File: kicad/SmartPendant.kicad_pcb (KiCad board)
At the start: 2 copper layers, 125 x 59 mm, 49 parts, among them J1 UART, J2 ST-LINK, J3 Encoder, J4 Display, J5 USB_C_Receptacle_USB2.0_16P, J6 Micro_SD_Card_Det1, Q1 MMBT3904, U1 WEACT BLACKPILL F4X1, U2 AMS1117-3.3, U3 MB85RC256VPNF-G-JNERE1

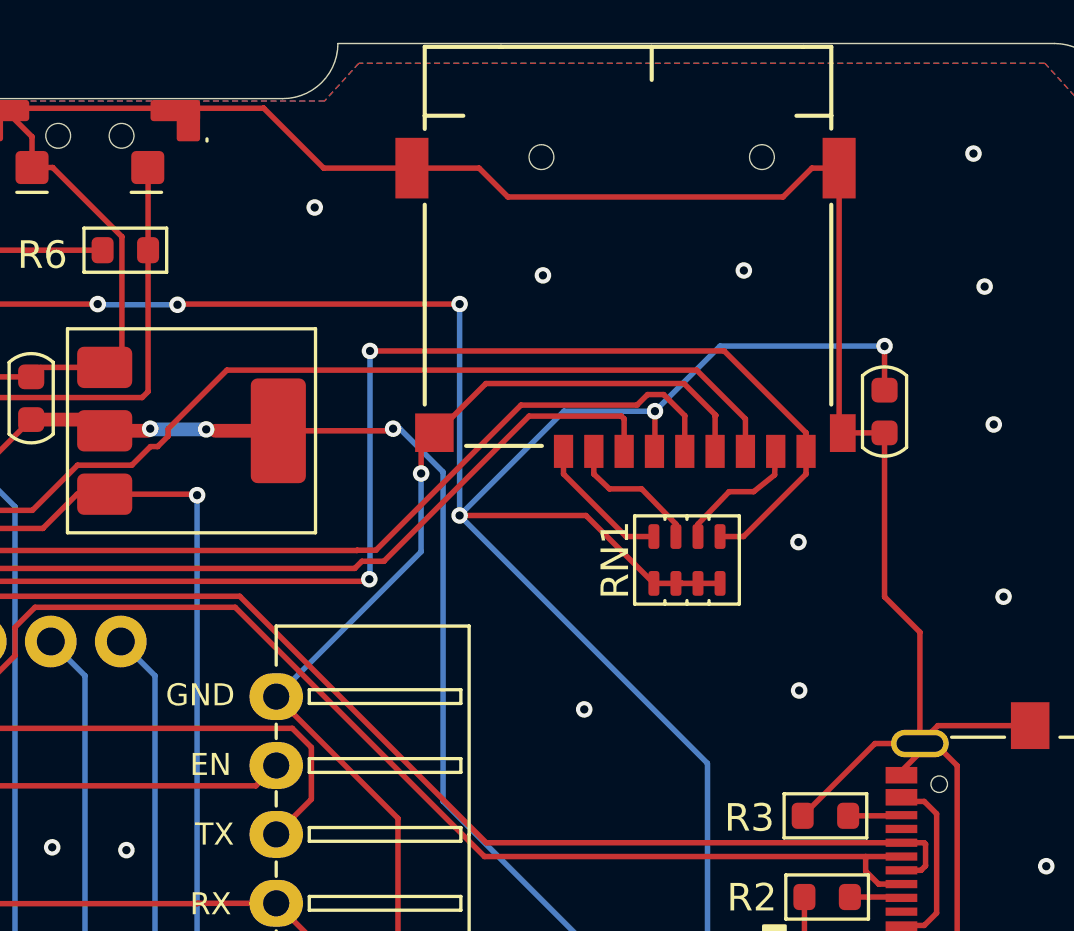
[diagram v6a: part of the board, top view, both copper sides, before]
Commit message: Use dual SD-card footprint.
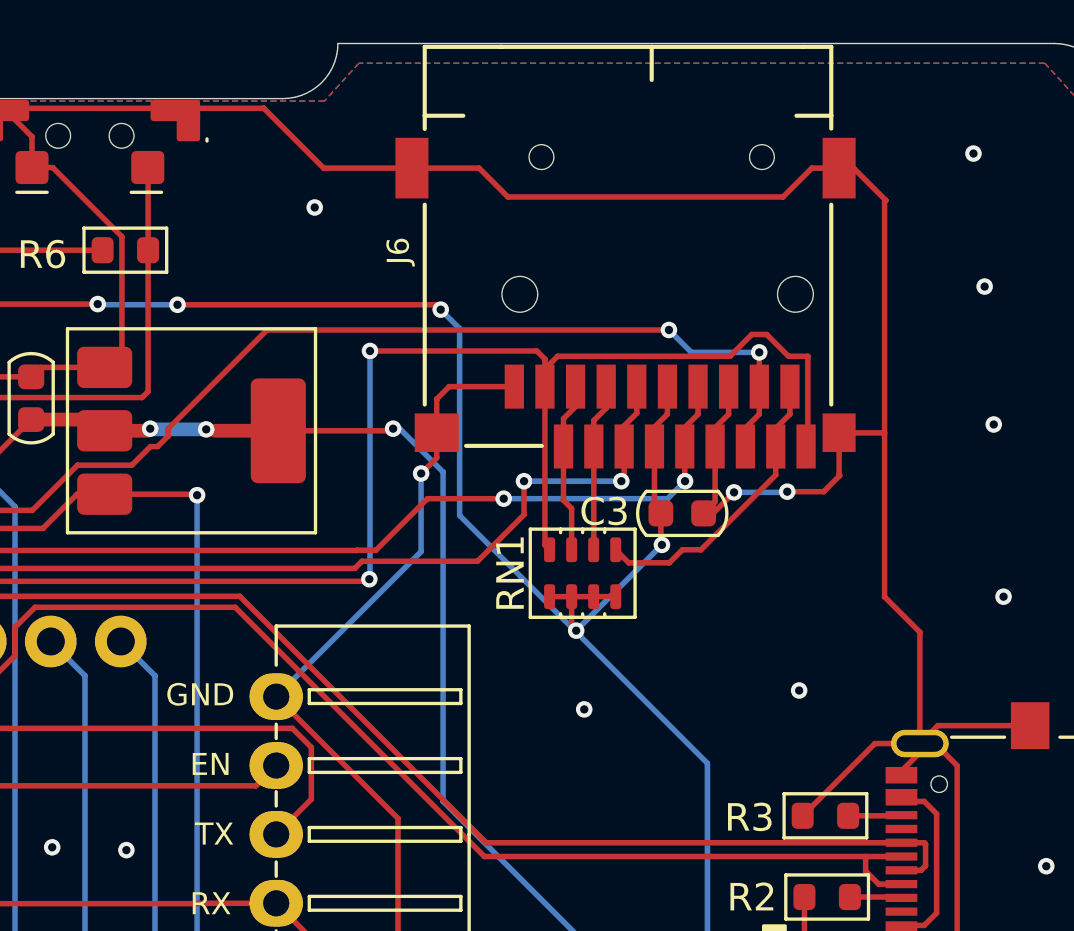
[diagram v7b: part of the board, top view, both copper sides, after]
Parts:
- J6: footprint Custom:J_SD_Card-micro_socket_A -> Custom:J_SD_Card-micro_dual
- moved C3 8.22 mm to (234.5, 65.0), turned to 0 degrees
- moved RN1 3.82 mm to (230.9, 67.2)
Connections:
- RN1 pad 5: SDIO_CD -> Net-(J6-DAT1)
- RN1 pad 6: Net-(J6-DAT1) -> Net-(J6-DAT3/CD)
- RN1 pad 7: Net-(J6-DAT3/CD) -> Net-(J6-DAT2)
- RN1 pad 8: Net-(J6-DAT2) -> SDIO_CD
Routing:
- net VCC: track 306.2 -> 288.4 mm, vias 15 -> 14
- net Net-(J6-DAT1): track 4.98 -> 10.7 mm
- net GND: track 410.3 -> 416.0 mm, vias 85 -> 84
- net SDIO_CD: track 47.4 -> 52.6 mm
- net SDIO_D0: track 67.1 -> 70.5 mm, vias 1 -> 3
- net SDIO_CMD: track 63.5 -> 65.8 mm, vias 1 -> 3
- net Net-(J6-DAT2): track 5.22 -> 6.23 mm
- net Net-(J6-DAT3/CD): track 5.18 -> 6.11 mm
- net SDIO_CK: track 35.1 -> 36.1 mm, vias 1 -> 3

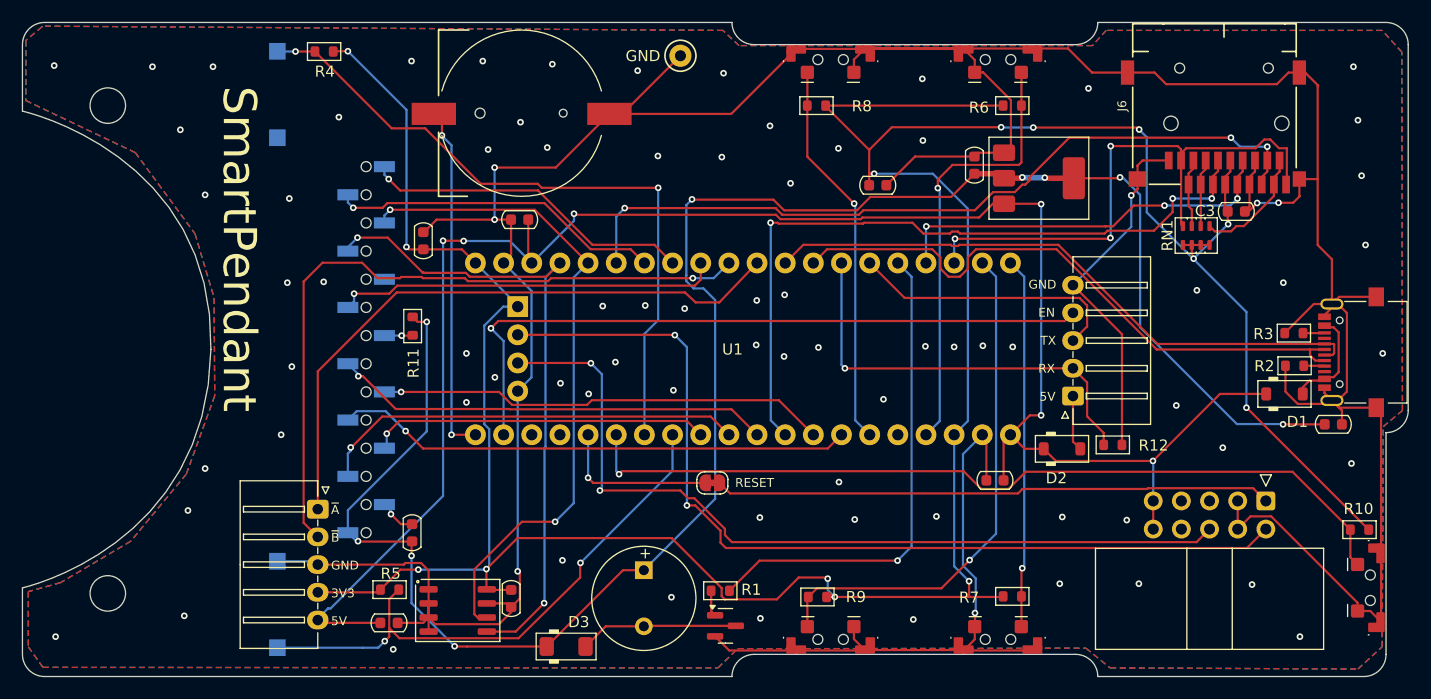
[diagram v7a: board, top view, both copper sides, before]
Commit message: Increase width of power tracks, add stitching vias.
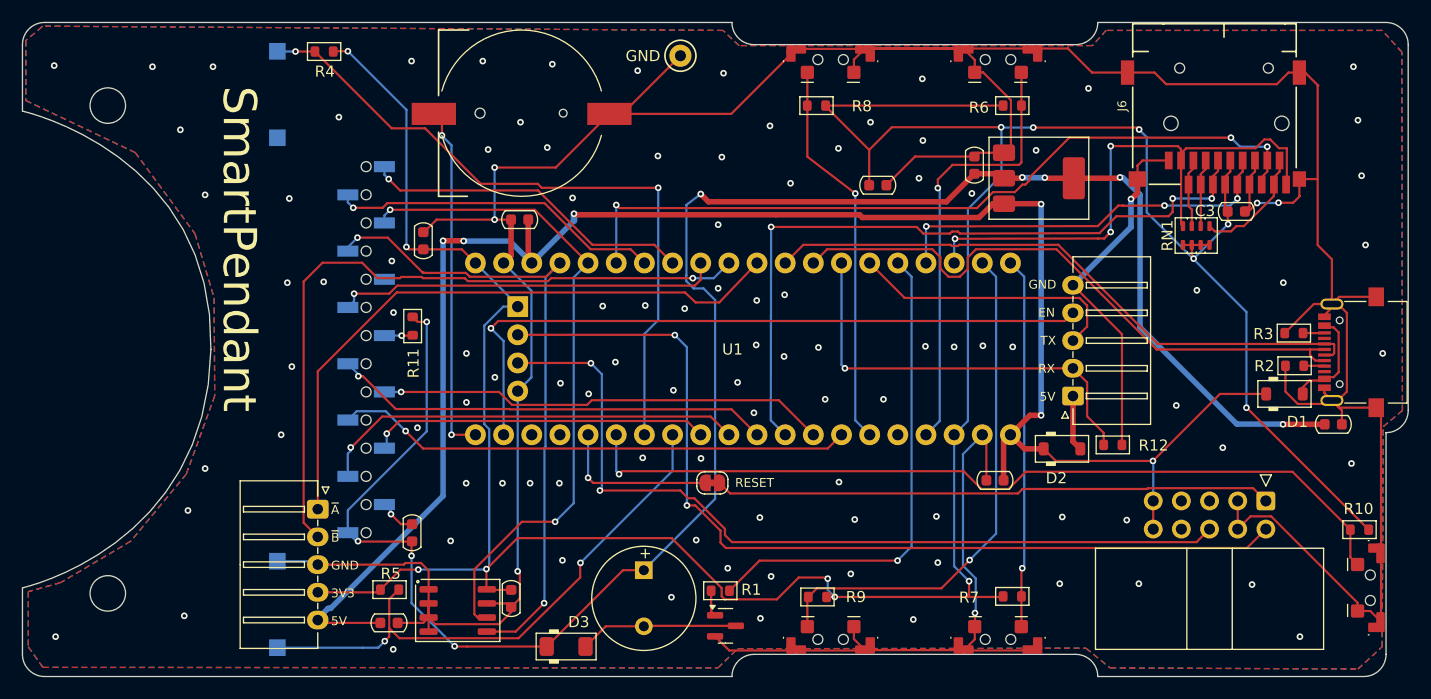
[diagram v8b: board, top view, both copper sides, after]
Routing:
- net VCC: track 288.4 -> 286.8 mm, vias 14 -> 13
- net SDIO_CMD: track 65.8 -> 65.1 mm
- net GND: vias 84 -> 109
